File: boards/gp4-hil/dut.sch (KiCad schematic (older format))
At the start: 1 part, among them P1 CONN_01X20

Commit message: Added FPGA core clock, GPIO indicator LEDs, expansion header, lots of test points
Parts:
- added C173: 4.7 uF, symbol C
- added C174: 0.47 uF, symbol C
- added D21, D22, D23, D24, D25, D26, D27, D28, D29, D30, D31, D32, D33, D34, D35, D36, D37, D38: GREEN, symbol LED
- added P2: GPAK_ZIF, symbol CONN_01X20
- added Q11, Q13, Q14, Q15, Q16, Q17, Q18, Q19, Q20, Q21: SSM6N58NU, symbol SSM6N58NU_DUAL_NMOS
- added R151, R152, R153, R154, R155, R156, R157, R158, R159, R160, R161, R162, R163, R164, R165, R166, R167, R168: 220, symbol R
- added TP1, TP10, TP11, TP12, TP13, TP14, TP15, TP16, TP17, TP18, TP19, TP2, TP20, TP21, TP3, TP33, TP4, TP5, TP6, TP7, TP8, TP9: TESTPOINT, symbol CONN_01X01
- added U32: SIP32408, symbol SIP32408
- P1: value CONN_01X20 -> GPAK_ZIF
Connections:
- net DUT_GPIO10: now also P2.10 (P10), Q20.G2 (G), TP12.1 (P1)
- net DUT_GPIO12: now also P2.12 (P12), Q13.G2 (G), TP13.1 (P1)
- net DUT_GPIO13: now also P2.13 (P13), Q14.G2 (G), TP14.1 (P1)
- net DUT_GPIO14: now also C174.1, P2.14 (P14), Q15.G2 (G), TP15.1 (P1), U32.4 (OUT)
- net DUT_GPIO15: now also P2.15 (P15), Q16.G2 (G), TP16.1 (P1)
- net DUT_GPIO16: now also P2.16 (P16), Q17.G2 (G), TP17.1 (P1)
- net DUT_GPIO17: now also P2.17 (P17), Q18.G2 (G), TP18.1 (P1)
- net DUT_GPIO18: now also P2.18 (P18), Q19.G2 (G), TP19.1 (P1)
- net DUT_GPIO19: now also P2.19 (P19), Q20.G1 (G), TP20.1 (P1)
- net DUT_GPIO2: now also Q13.G1 (G), TP4.1 (P1)
- net DUT_GPIO20: now also P2.20 (P20), Q21.G1 (G), TP21.1 (P1)
- net DUT_GPIO3: now also P2.3 (P3), Q14.G1 (G), TP5.1 (P1)
- net DUT_GPIO4: now also P2.4 (P4), Q15.G1 (G), TP6.1 (P1)
- net DUT_GPIO5: now also P2.5 (P5), Q16.G1 (G), TP7.1 (P1)
- net DUT_GPIO6: now also P2.6 (P6), Q17.G1 (G), TP8.1 (P1)
- net DUT_GPIO7: now also P2.7 (P7), Q18.G1 (G), TP9.1 (P1)
- net DUT_GPIO8: now also P2.8 (P8), Q19.G1 (G), TP10.1 (P1)
- net DUT_GPIO9: now also P2.9 (P9), Q11.G2 (G), TP11.1 (P1)
- net DUT_VDD1: now also P2.1 (P1), TP1.1 (P1)
- net DUT_VDD2: now also C173.1, TP2.1 (P1), U32.1 (IN)
- net GND: now also C173.2, C174.2, P2.11 (P11), Q11.S2 (S), Q13.S1 (S), Q13.S2 (S), Q14.S1 (S), Q14.S2 (S), Q15.S1 (S), Q15.S2 (S), Q16.S1 (S), Q16.S2 (S), Q17.S1 (S), Q17.S2 (S), Q18.S1 (S), Q18.S2 (S), Q19.S1 (S), Q19.S2 (S), Q20.S1 (S), Q20.S2 (S), Q21.S1 (S), TP3.1 (P1), U32.2 (GND), U32.PAD (GND)
- new net: Q13.D1 (D), R151.1
- new net: D21.1 (K), R151.2
- new net: Q14.D1 (D), R153.1
- new net: D23.1 (K), R153.2
- new net: Q15.D1 (D), R155.1
- new net: D25.1 (K), R155.2
- new net: Q16.D1 (D), R157.1
- new net: D27.1 (K), R157.2
- new net: Q17.D1 (D), R159.1
- new net: D29.1 (K), R159.2
- new net: Q18.D1 (D), R161.1
- new net: D31.1 (K), R161.2
- new net: Q19.D1 (D), R163.1
- new net: D33.1 (K), R163.2
- new net: Q11.D2 (D), R165.1
- new net: D35.1 (K), R165.2
- new net: Q20.D2 (D), R167.1
- new net: D37.1 (K), R167.2
- new net: Q13.D2 (D), R152.1
- new net: D22.1 (K), R152.2
- new net: Q14.D2 (D), R154.1
- new net: D24.1 (K), R154.2
- new net: Q15.D2 (D), R156.1
- new net: D26.1 (K), R156.2
- new net: Q16.D2 (D), R158.1
- new net: D28.1 (K), R158.2
- new net: Q17.D2 (D), R160.1
- new net: D30.1 (K), R160.2
- new net: Q18.D2 (D), R162.1
- new net: D32.1 (K), R162.2
- new net: Q19.D2 (D), R164.1
- new net: D34.1 (K), R164.2
- new net: Q20.D1 (D), R166.1
- new net: D36.1 (K), R166.2
- new net: Q21.D1 (D), R168.1
- new net: D38.1 (K), R168.2
- new net 3V3: D21.2 (A), D22.2 (A), D23.2 (A), D24.2 (A), D25.2 (A), D26.2 (A), D27.2 (A), D28.2 (A), D29.2 (A), D30.2 (A), D31.2 (A), D32.2 (A), D33.2 (A), D34.2 (A), D35.2 (A), D36.2 (A), D37.2 (A), D38.2 (A)
- new net DUT_VDD2_EN: TP33.1 (P1), U32.3 (EN)
- new net GPIO2_DIO: P2.2 (P2)
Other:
- note added: "Buffered indicator LEDs"
- note added: "Note that pin 2 is connected to FPGA-side\nsignal to isolate it from Vpp"
- note removed: "TODO: Buffered indicator LEDs"
- note removed: "TODO: Expansion header of some sort\nTODO: Probe clips on every pin"
- note removed: "TODO: Pass transistor to enable DUT_VDD2"
- note removed: "Total number of switches needed:\n* 18 GPIO -> FPGA\n* 15 GPIO -> DAC\n* 2 Vdd -> regulator\n\nADC is always connected\n\nNeed >8V compatible switch (in open state) for FPGA->GPIO2"

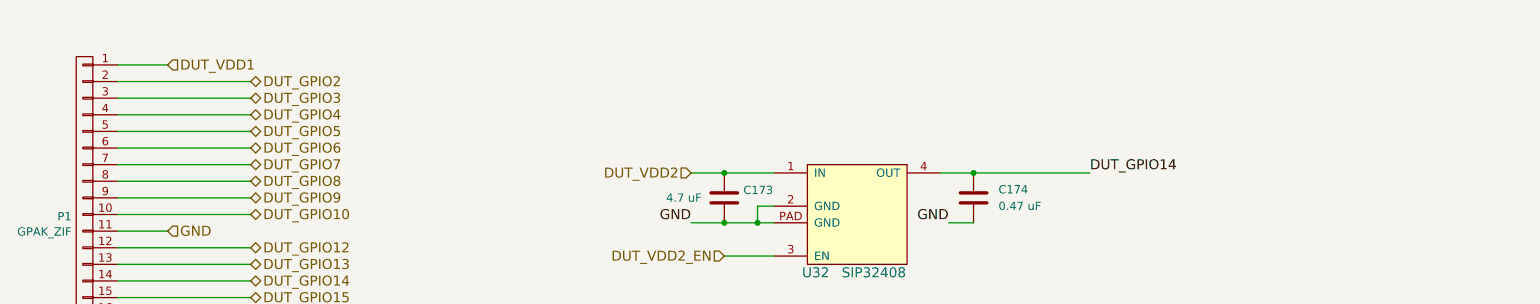
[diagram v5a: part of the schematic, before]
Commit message: Added current monitoring shunts. Began design review
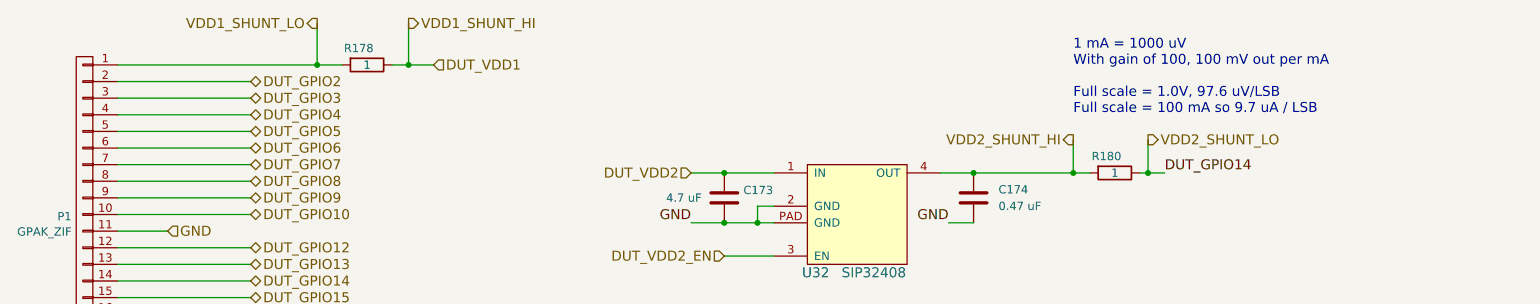
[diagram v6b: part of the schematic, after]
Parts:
- added R178, R180: 1, symbol R
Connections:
- net DUT_GPIO14: now also R180.1; no longer C174.1, U32.4 (OUT)
- net DUT_VDD1: now also R178.1; no longer P1.1 (P1)
- new net VDD1_SHUNT_LO: P1.1 (P1), R178.2
- new net VDD2_SHUNT_HI: C174.1, R180.2, U32.4 (OUT)
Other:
- note added: "1 mA = 1000 uV\nWith gain of 100, 100 mV out per mA\n\nFull scale = 1.0V, 97.6 uV/LSB\nFull scale = 100 mA so 9.7 uA / LSB"

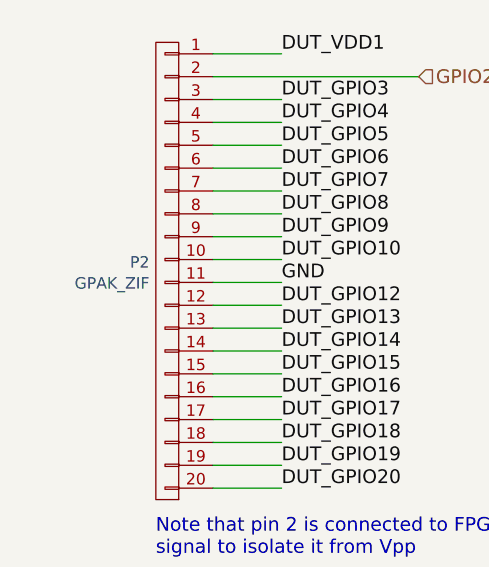
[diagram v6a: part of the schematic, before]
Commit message: Added shunt amplifiers and connected to ADC
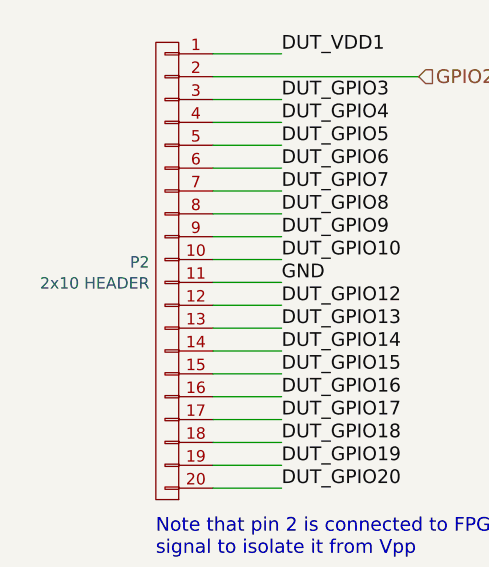
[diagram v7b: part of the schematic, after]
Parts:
- P2: value GPAK_ZIF -> 2x10 HEADER
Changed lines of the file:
@@
 Sheet 4 7
 Title "GreenPak Hardware-In-Loop Test Platform"
-Date "2016-05-18"
+Date "2016-05-19"
 Rev "0.1"
 Comp "Andrew Zonenberg"
@@
 P 1400 4350
 F 0 "P2" H 1478 4388 50  0000 L CNN
-F 1 "GPAK_ZIF" H 1478 4296 50  0000 L CNN
+F 1 "2x10 HEADER" H 1478 4296 50  0000 L CNN
 F 2 "" H 1400 4350 60  0000 C CNN
 F 3 "" H 1400 4350 60  0000 C CNN

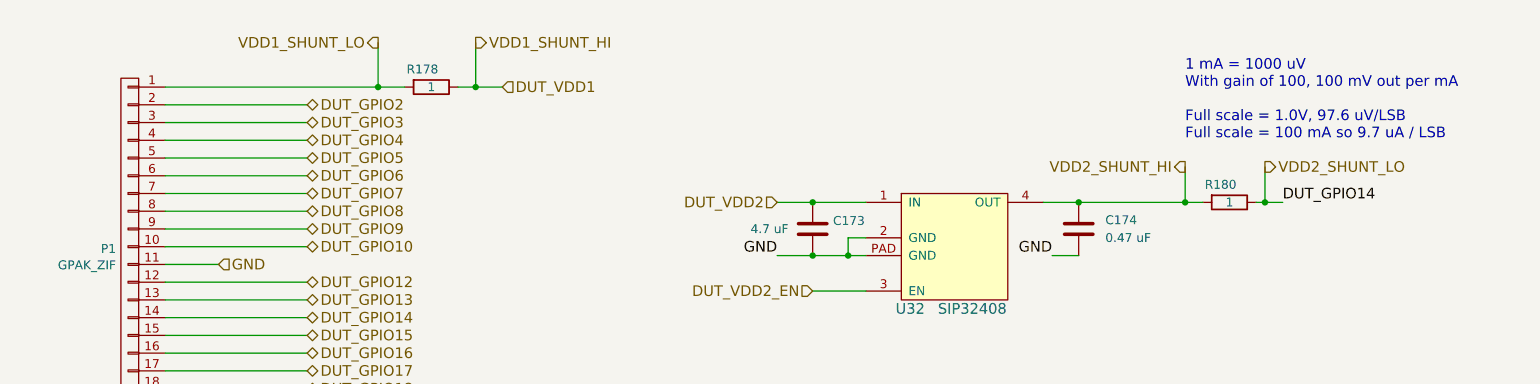
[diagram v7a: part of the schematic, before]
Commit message: Added post-shunt decoupling caps to DUT_VDDx rails
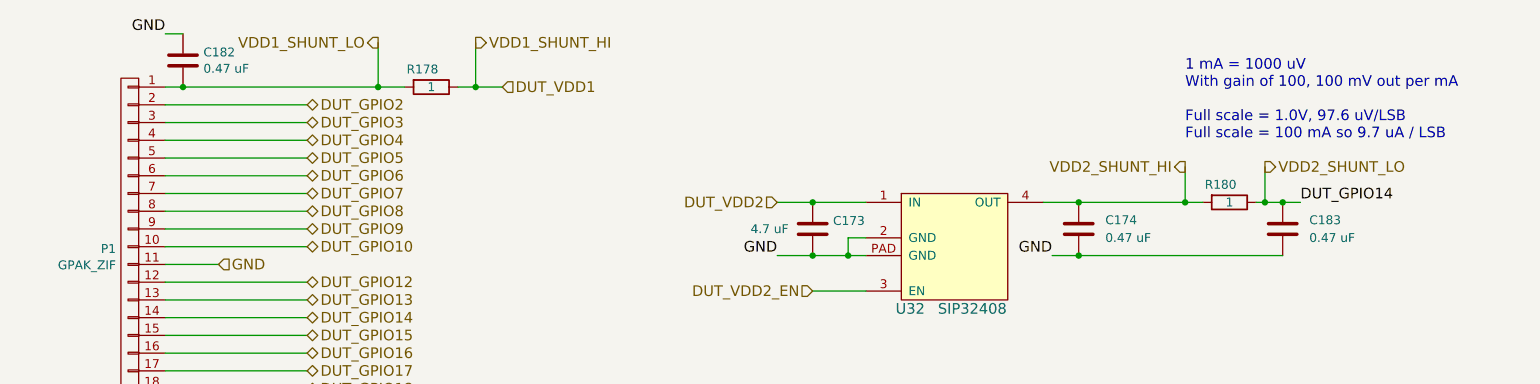
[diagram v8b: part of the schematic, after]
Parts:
- added C182, C183: 0.47 uF, symbol C
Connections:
- net DUT_GPIO14: now also C183.1
- net GND: now also C182.1, C183.2
- net VDD1_SHUNT_LO: now also C182.2
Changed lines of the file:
@@
 Text HLabel 5050 1600 0    60   Input ~ 0
 DUT_VDD2
-Text Label 7900 1600 0    60   ~ 0
+Text Label 8000 1600 0    60   ~ 0
 DUT_GPIO14
 Text HLabel 5250 2100 0    60   Input ~ 0
@@
 	6550 1600 7450 1600
 Wire Wire Line
-	6600 1900 6750 1900
+	6600 1900 7900 1900
 Wire Wire Line
 	5250 2100 5550 2100
@@
 Connection ~ 6550 8150
 Wire Wire Line
-	3500 950  3250 950
+	3250 950  3500 950
 Wire Wire Line
 	3350 700  3350 950
@@
 $EndComp
 Wire Wire Line
-	7900 1600 7750 1600
+	7750 1600 8000 1600
 Wire Wire Line
 	7350 1400 7350 1600
@@
 Text Notes 7350 1250 0    60   ~ 0
 1 mA = 1000 uV\nWith gain of 100, 100 mV out per mA\n\nFull scale = 1.0V, 97.6 uV/LSB\nFull scale = 100 mA so 9.7 uA / LSB
+$Comp
+L C C182
+U 1 1 577334C7
+P 1700 800
+F 0 "C182" H 1815 846 50  0000 L CNN
+F 1 "0.47 uF" H 1815 754 50  0000 L CNN
+F 2 "" H 1738 650 30  0000 C CNN
+F 3 "" H 1700 800 60  0000 C CNN
+	1    1700 800
+	1    0    0    -1
+$EndComp
+Connection ~ 1700 950
+Text Label 1600 650  2    60   ~ 0
+GND
+Wire Wire Line
+	1600 650  1700 650
+$Comp
+L C C183
+U 1 1 57734A4F
+P 7900 1750
+F 0 "C183" H 8050 1800 50  0000 L CNN
+F 1 "0.47 uF" H 8050 1700 50  0000 L CNN
+F 2 "" H 7938 1600 30  0000 C CNN
+F 3 "" H 7900 1750 60  0000 C CNN
+	1    7900 1750
+	1    0    0    -1
+$EndComp
+Connection ~ 7900 1600
+Connection ~ 6750 1900
 $EndSCHEMATC
